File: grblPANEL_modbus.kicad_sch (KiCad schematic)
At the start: 14 parts, among them J401 Conn_01x02, U401 THVD1406

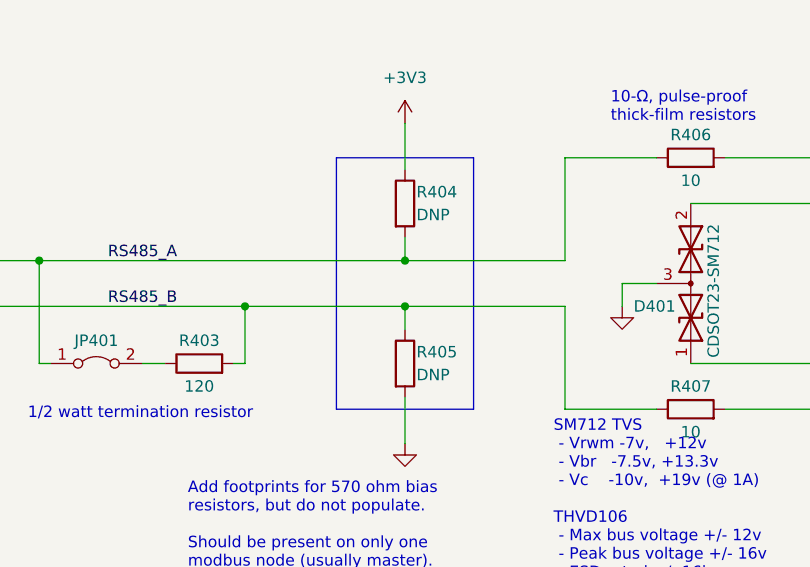
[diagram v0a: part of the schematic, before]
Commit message: Place and route changes from schematic
Headers for serial console.
DNP components to v7 format.
Power status components.
LEDs to bottom side, plus silkscreen.
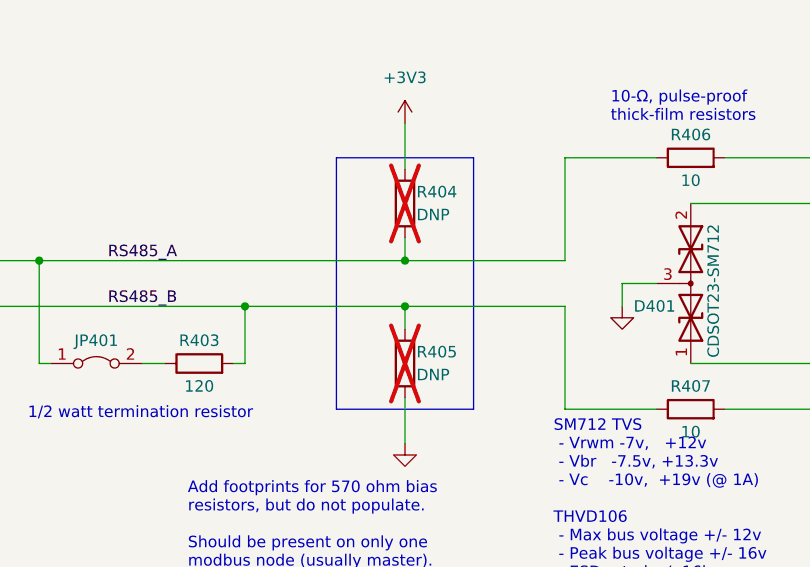
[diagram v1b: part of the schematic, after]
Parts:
- R404, R405: now not fitted
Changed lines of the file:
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@@
   )
   (symbol (lib_id "Device:R") (at 176.53 67.31 0) (unit 1)
-    (in_bom yes) (on_board yes) (dnp no)
+    (in_bom yes) (on_board yes) (dnp yes)
     (property "Reference" "R404" (at 177.8 66.04 0)
       (effects (font (size 1.27 1.27)) (justify left))
@@
   )
   (symbol (lib_id "Device:R") (at 176.53 85.09 0) (unit 1)
-    (in_bom yes) (on_board yes) (dnp no)
+    (in_bom yes) (on_board yes) (dnp yes)
     (property "Reference" "R405" (at 177.8 83.82 0)
       (effects (font (size 1.27 1.27)) (justify left))
